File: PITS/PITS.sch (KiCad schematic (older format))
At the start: 47 parts, among them P1 CONN_02X20, P10 I2C, P11 I2C, P12 I2C, P13 I2C, P14 BATT, P2 BNC, P3 BNC, P4 BNC, P5 BNC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

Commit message: layout - work in progress - backup GPS antenne change
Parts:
- P2: footprint Connectors:SMA_Edge_small -> RF_Modules:MWSL1252
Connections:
- net GPIO22: now also D1.2 (A); no longer U4.14 (DIO0)
- net GPIO23: now also U4.14 (DIO0)
- net GPIO24: now also D2.2 (A)
- net GPIO25: now also U4.7 (DIO5)
- net GPIO27: no longer U4.7 (DIO5)
- net GPIO7(CE1): no longer U4.5 (nSS)
- net GPIO8(CE0): now also U4.5 (nSS)
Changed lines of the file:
@@
 Text Label 7100 1100 2    60   ~ 0
 GPIO10(MOSI0)
-Text Label 7000 1300 2    60   ~ 0
-GPIO7(CE1)
 Text Notes 9650 2550 2    100  ~ 20
 LORA/RFM9*
@@
 F 0 "P2" H 810 1120 50  0000 C CNN
 F 1 "BNC" V 910 940 50  0000 C CNN
-F 2 "Connectors:SMA_Edge_small" H 800 1000 50  0001 C CNN
+F 2 "RF_Modules:MWSL1252" H 800 1000 50  0001 C CNN
 F 3 "" H 800 1000 50  0000 C CNN
 	1    800  1000
@@
 Wire Wire Line
 	3500 1600 4100 1600
-Text Label 6900 2000 2    60   ~ 0
-GPIO27
-Text Label 6900 1500 2    60   ~ 0
+Text Label 2800 2900 2    60   ~ 0
 GPIO22
 $Comp
@@
 Text Label 2800 4100 2    60   ~ 0
 GPIO7(CE1)
+Text Label 7000 1300 2    60   ~ 0
+GPIO8(CE0)
+Text Label 2800 3300 2    60   ~ 0
+GPIO24
+Text Label 6900 2000 2    60   ~ 0
+GPIO25
+Text Label 6900 1500 2    60   ~ 0
+GPIO23
 $EndSCHEMATC

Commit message: layout - work in progress - RFM, LEDs, UBLOX
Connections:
- net D1: now also D1.2 (A), R14.2; no longer D1.1 (K), R14.1
- net D2: now also D2.2 (A), R15.2; no longer D2.1 (K), R15.1
- net D3: now also D3.2 (A), R20.2; no longer D3.1 (K), R20.1
- net D4: now also D4.2 (A), R21.2; no longer D4.1 (K), R21.1
- net D5: now also D5.2 (A), R22.2; no longer D5.1 (K), R22.1
- net D6: now also D6.2 (A), R23.2; no longer D6.1 (K), R23.1
- net GND: now also D1.1 (K), D2.1 (K), D3.1 (K), D4.1 (K), D5.1 (K), D6.1 (K); no longer R14.2, R15.2, R20.2, R21.2, R22.2, R23.2
- net GPIO12: no longer D3.2 (A)
- net GPIO13: now also R26.1
- net GPIO17: now also U4.14 (DIO0); no longer U3.4 (EN/PGM)
- net GPIO18: now also R14.1; no longer R26.1
- net GPIO22: now also R21.1; no longer D1.2 (A)
- net GPIO23: now also R20.1; no longer U4.14 (DIO0)
- net GPIO24: now also R22.1; no longer D2.2 (A)
- net GPIO25: now also R23.1; no longer U4.7 (DIO5)
- net GPIO27: now also R15.1
- net GPIO5: no longer D5.2 (A)
- net GPIO6: no longer D6.2 (A)
- net GPIO7(CE1): now also U4.5 (nSS); no longer D4.2 (A)
- net GPIO8(CE0): now also U4.7 (DIO5); no longer U4.5 (nSS)
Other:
- moved on the sheet: D1, D2, D3, D4, D5, D6, R14, R15, R20, R21, R22, R23
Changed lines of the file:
@@
 L LED D1
 U 1 1 58198207
-P 1700 2900
-F 0 "D1" H 1700 3000 50  0000 C CNN
-F 1 "OK_Green" H 1700 2800 50  0000 C CNN
-F 2 "LEDs:LED_0603" H 1700 2900 50  0001 C CNN
-F 3 "" H 1700 2900 50  0000 C CNN
-	1    1700 2900
+P 1200 2900
+F 0 "D1" H 1200 3000 50  0000 C CNN
+F 1 "OK_Green" H 1200 2800 50  0000 C CNN
+F 2 "LEDs:LED_0603" H 1200 2900 50  0001 C CNN
+F 3 "" H 1200 2900 50  0000 C CNN
+	1    1200 2900
 	1    0    0    -1
 $EndComp
@@
 L LED D2
 U 1 1 5819820E
-P 1700 3300
-F 0 "D2" H 1700 3400 50  0000 C CNN
-F 1 "WARN_Red" H 1700 3200 50  0000 C CNN
-F 2 "LEDs:LED_0603" H 1700 3300 50  0001 C CNN
-F 3 "" H 1700 3300 50  0000 C CNN
-	1    1700 3300
+P 1200 3300
+F 0 "D2" H 1200 3400 50  0000 C CNN
+F 1 "WARN_Red" H 1200 3200 50  0000 C CNN
+F 2 "LEDs:LED_0603" H 1200 3300 50  0001 C CNN
+F 3 "" H 1200 3300 50  0000 C CNN
+	1    1200 3300
 	1    0    0    -1
 $EndComp
@@
 L LED D3
 U 1 1 58198215
-P 1700 3700
-F 0 "D3" H 1700 3800 50  0000 C CNN
-F 1 "Inet_Green" H 1700 3600 50  0000 C CNN
-F 2 "LEDs:LED_0603" H 1700 3700 50  0001 C CNN
-F 3 "" H 1700 3700 50  0000 C CNN
-	1    1700 3700
+P 1200 3700
+F 0 "D3" H 1200 3800 50  0000 C CNN
+F 1 "Inet_Green" H 1200 3600 50  0000 C CNN
+F 2 "LEDs:LED_0603" H 1200 3700 50  0001 C CNN
+F 3 "" H 1200 3700 50  0000 C CNN
+	1    1200 3700
 	1    0    0    -1
 $EndComp
@@
 L R R14
 U 1 1 581983DD
-P 1150 2900
-F 0 "R14" V 1230 2900 50  0000 C CNN
-F 1 "330" V 1150 2900 50  0000 C CNN
-F 2 "Resistors_SMD:R_0603_HandSoldering" V 1080 2900 50  0001 C CNN
-F 3 "" H 1150 2900 50  0000 C CNN
-	1    1150 2900
+P 1750 2900
+F 0 "R14" V 1830 2900 50  0000 C CNN
+F 1 "330" V 1750 2900 50  0000 C CNN
+F 2 "Resistors_SMD:R_0603_HandSoldering" V 1680 2900 50  0001 C CNN
+F 3 "" H 1750 2900 50  0000 C CNN
+	1    1750 2900
 	0    1    1    0
 $EndComp
@@
 L R R15
 U 1 1 58198843
-P 1150 3300
-F 0 "R15" V 1230 3300 50  0000 C CNN
-F 1 "330" V 1150 3300 50  0000 C CNN
-F 2 "Resistors_SMD:R_0603_HandSoldering" V 1080 3300 50  0001 C CNN
-F 3 "" H 1150 3300 50  0000 C CNN
-	1    1150 3300
+P 1750 3300
+F 0 "R15" V 1830 3300 50  0000 C CNN
+F 1 "330" V 1750 3300 50  0000 C CNN
+F 2 "Resistors_SMD:R_0603_HandSoldering" V 1680 3300 50  0001 C CNN
+F 3 "" H 1750 3300 50  0000 C CNN
+	1    1750 3300
 	0    1    1    0
 $EndComp
@@
 L R R20
 U 1 1 581988DE
-P 1150 3700
-F 0 "R20" V 1230 3700 50  0000 C CNN
-F 1 "330" V 1150 3700 50  0000 C CNN
-F 2 "Resistors_SMD:R_0603_HandSoldering" V 1080 3700 50  0001 C CNN
-F 3 "" H 1150 3700 50  0000 C CNN
-	1    1150 3700
+P 1750 3700
+F 0 "R20" V 1830 3700 50  0000 C CNN
+F 1 "330" V 1750 3700 50  0000 C CNN
+F 2 "Resistors_SMD:R_0603_HandSoldering" V 1680 3700 50  0001 C CNN
+F 3 "" H 1750 3700 50  0000 C CNN
+	1    1750 3700
 	0    1    1    0
 $EndComp
@@
 L LED D4
 U 1 1 5819A39B
-P 1700 4100
-F 0 "D4" H 1700 4200 50  0000 C CNN
-F 1 "LAN_Yellow" H 1700 4000 50  0000 C CNN
-F 2 "LEDs:LED_0603" H 1700 4100 50  0001 C CNN
-F 3 "" H 1700 4100 50  0000 C CNN
-	1    1700 4100
+P 1200 4100
+F 0 "D4" H 1200 4200 50  0000 C CNN
+F 1 "LAN_Yellow" H 1200 4000 50  0000 C CNN
+F 2 "LEDs:LED_0603" H 1200 4100 50  0001 C CNN
+F 3 "" H 1200 4100 50  0000 C CNN
+	1    1200 4100
 	1    0    0    -1
 $EndComp
@@
 L LED D5
 U 1 1 5819A3A2
-P 1700 4500
-F 0 "D5" H 1700 4600 50  0000 C CNN
-F 1 "DATA0_Red" H 1700 4400 50  0000 C CNN
-F 2 "LEDs:LED_0603" H 1700 4500 50  0001 C CNN
-F 3 "" H 1700 4500 50  0000 C CNN
-	1    1700 4500
+P 1200 4500
+F 0 "D5" H 1200 4600 50  0000 C CNN
+F 1 "DATA0_Red" H 1200 4400 50  0000 C CNN
+F 2 "LEDs:LED_0603" H 1200 4500 50  0001 C CNN
+F 3 "" H 1200 4500 50  0000 C CNN
+	1    1200 4500
 	1    0    0    -1
 $EndComp
@@
 L LED D6
 U 1 1 5819A3A9
-P 1700 4900
-F 0 "D6" H 1700 5000 50  0000 C CNN
-F 1 "DATA1_Red" H 1700 4800 50  0000 C CNN
-F 2 "LEDs:LED_0603" H 1700 4900 50  0001 C CNN
-F 3 "" H 1700 4900 50  0000 C CNN
-	1    1700 4900
+P 1200 4900
+F 0 "D6" H 1200 5000 50  0000 C CNN
+F 1 "DATA1_Red" H 1200 4800 50  0000 C CNN
+F 2 "LEDs:LED_0603" H 1200 4900 50  0001 C CNN
+F 3 "" H 1200 4900 50  0000 C CNN
+	1    1200 4900
 	1    0    0    -1
 $EndComp
@@
 L R R21
 U 1 1 5819A3B0
-P 1150 4100
-F 0 "R21" V 1230 4100 50  0000 C CNN
-F 1 "330" V 1150 4100 50  0000 C CNN
-F 2 "Resistors_SMD:R_0603_HandSoldering" V 1080 4100 50  0001 C CNN
-F 3 "" H 1150 4100 50  0000 C CNN
-	1    1150 4100
+P 1750 4100
+F 0 "R21" V 1830 4100 50  0000 C CNN
+F 1 "330" V 1750 4100 50  0000 C CNN
+F 2 "Resistors_SMD:R_0603_HandSoldering" V 1680 4100 50  0001 C CNN
+F 3 "" H 1750 4100 50  0000 C CNN
+	1    1750 4100
 	0    1    1    0
 $EndComp
@@
 L R R22
 U 1 1 5819A3B7
-P 1150 4500
-F 0 "R22" V 1230 4500 50  0000 C CNN
-F 1 "330" V 1150 4500 50  0000 C CNN
-F 2 "Resistors_SMD:R_0603_HandSoldering" V 1080 4500 50  0001 C CNN
-F 3 "" H 1150 4500 50  0000 C CNN
-	1    1150 4500
+P 1750 4500
+F 0 "R22" V 1830 4500 50  0000 C CNN
+F 1 "330" V 1750 4500 50  0000 C CNN
+F 2 "Resistors_SMD:R_0603_HandSoldering" V 1680 4500 50  0001 C CNN
+F 3 "" H 1750 4500 50  0000 C CNN
+	1    1750 4500
 	0    1    1    0
 $EndComp
@@
 L R R23
 U 1 1 5819A3BE
-P 1150 4900
-F 0 "R23" V 1230 4900 50  0000 C CNN
-F 1 "330" V 1150 4900 50  0000 C CNN
-F 2 "Resistors_SMD:R_0603_HandSoldering" V 1080 4900 50  0001 C CNN
-F 3 "" H 1150 4900 50  0000 C CNN
-	1    1150 4900
+P 1750 4900
+F 0 "R23" V 1830 4900 50  0000 C CNN
+F 1 "330" V 1750 4900 50  0000 C CNN
+F 2 "Resistors_SMD:R_0603_HandSoldering" V 1680 4900 50  0001 C CNN
+F 3 "" H 1750 4900 50  0000 C CNN
+	1    1750 4900
 	0    1    1    0
 $EndComp
@@
 Text Label 4300 1300 2    60   ~ 0
 GPIO19(MISO1)
-Text Label 2800 4900 2    60   ~ 0
-GPIO6
-Text Label 2800 4500 2    60   ~ 0
-GPIO5
 Text Label 9800 4100 2    60   ~ 0
 GPIO2(SDA1)
@@
 	0    1    1    0
 $EndComp
-Text Label 6800 6100 2    60   ~ 0
-GPIO17
 Text Label 6800 6000 2    60   ~ 0
 GPIO14(TXD0)
-Text Label 3300 6100 2    60   ~ 0
-GPIO18
 Text Notes 6850 7050 2    100  ~ 20
 UKHAS
@@
 Connection ~ 4000 4200
 Wire Wire Line
-	1300 2900 1500 2900
-Wire Wire Line
-	1500 3300 1300 3300
-Wire Wire Line
-	1300 3700 1500 3700
+	1400 2900 1600 2900
+Wire Wire Line
+	1600 3300 1400 3300
+Wire Wire Line
+	1400 3700 1600 3700
 Wire Wire Line
 	900  2900 1000 2900
@@
 	900  3700 1000 3700
 Wire Wire Line
-	1300 4100 1500 4100
-Wire Wire Line
-	1500 4500 1300 4500
-Wire Wire Line
-	1300 4900 1500 4900
+	1400 4100 1600 4100
+Wire Wire Line
+	1600 4500 1400 4500
+Wire Wire Line
+	1400 4900 1600 4900
 Wire Wire Line
 	900  4100 1000 4100
@@
 Wire Wire Line
 	3500 1600 4100 1600
-Text Label 2800 2900 2    60   ~ 0
+Text Label 2800 4100 2    60   ~ 0
 GPIO22
 $Comp
@@
 Text Label 2500 6100 0    30   ~ 0
 HX1-TXD
-Text Label 1400 2900 0    30   ~ 0
+Text Label 1500 2900 0    30   ~ 0
 D1
-Text Label 1400 3300 0    30   ~ 0
+Text Label 1500 3300 0    30   ~ 0
 D2
-Text Label 1400 3700 0    30   ~ 0
+Text Label 1500 3700 0    30   ~ 0
 D3
-Text Label 1400 4100 0    30   ~ 0
+Text Label 1500 4100 0    30   ~ 0
 D4
-Text Label 1400 4500 0    30   ~ 0
+Text Label 1500 4500 0    30   ~ 0
 D5
-Text Label 1400 4900 0    30   ~ 0
+Text Label 1500 4900 0    30   ~ 0
 D6
 $Comp
@@
 	1    0    0    -1
 $EndComp
+Text Label 6900 2000 2    60   ~ 0
+GPIO8(CE0)
+Text Label 2800 4500 2    60   ~ 0
+GPIO24
+Text Label 7000 1300 2    60   ~ 0
+GPIO7(CE1)
+Text Label 3300 6100 2    60   ~ 0
+GPIO13
+Text Label 6900 1500 2    60   ~ 0
+GPIO17
+Text Label 2800 4900 2    60   ~ 0
+GPIO25
 Text Label 2800 3700 2    60   ~ 0
-GPIO12
-Text Label 2800 4100 2    60   ~ 0
-GPIO7(CE1)
-Text Label 7000 1300 2    60   ~ 0
-GPIO8(CE0)
+GPIO23
 Text Label 2800 3300 2    60   ~ 0
-GPIO24
-Text Label 6900 2000 2    60   ~ 0
-GPIO25
-Text Label 6900 1500 2    60   ~ 0
-GPIO23
+GPIO27
+Text Label 2800 2900 2    60   ~ 0
+GPIO18
 $EndSCHEMATC

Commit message: neue Pinbelegung
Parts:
- removed R5: 10k, Resistors_SMD:R_0603_HandSoldering, symbol R
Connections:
- net GPIO12: no longer U2.4 (TimePulse)
- net GPIO14(TXD0): no longer U2.3 (RXD)
- net GPIO15(RXD0): no longer U2.2 (TXD)
- net GPIO16(CE2): no longer U2.17 (SCL)
- net GPIO17: now also U2.4 (TimePulse); no longer U4.14 (DIO0)
- net GPIO18: now also U2.16 (SDA); no longer R14.1
- net GPIO19(MISO1): no longer U2.16 (SDA)
- net GPIO22: now also U1.4 (EN); no longer R21.1
- net GPIO23: now also R14.1; no longer R20.1
- net GPIO24: now also R15.1; no longer R22.1
- net GPIO25: now also R20.1; no longer R23.1, U1.4 (EN)
- net GPIO27: now also U4.14 (DIO0); no longer R15.1
- net GPIO4: now also U2.17 (SCL)
- no-connect marks 10 -> 12
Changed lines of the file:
@@
 	0    1    1    0
 $EndComp
-Text Label 4300 1300 2    60   ~ 0
-GPIO19(MISO1)
 Text Label 9800 4100 2    60   ~ 0
 GPIO2(SDA1)
@@
 	0    1    1    0
 $EndComp
-Text Label 6800 6000 2    60   ~ 0
-GPIO14(TXD0)
 Text Notes 6850 7050 2    100  ~ 20
 UKHAS
@@
 	1    0    0    -1
 $EndComp
-Text Label 4500 1100 2    60   ~ 0
-GPIO14(TXD0)
-Text Label 4500 1000 2    60   ~ 0
-GPIO15(RXD0)
-$Comp
-L R R5
-U 1 1 581C7F21
-P 3950 800
-F 0 "R5" V 4030 800 50  0000 C CNN
-F 1 "10k" V 3950 800 50  0000 C CNN
-F 2 "Resistors_SMD:R_0603_HandSoldering" V 3880 800 50  0001 C CNN
-F 3 "" H 3950 800 50  0000 C CNN
-	1    3950 800
-	0    1    1    0
-$EndComp
-Text Label 4500 800  2    60   ~ 0
-GPIO17
 Text Notes 4550 2550 2    100  ~ 20
 GPS
@@
 	2500 6100 2600 6100
 Wire Wire Line
-	6100 6000 6800 6000
-Wire Wire Line
 	2900 6100 3300 6100
 Wire Wire Line
@@
 Wire Wire Line
 	800  1200 800  2200
-Wire Wire Line
-	3500 1100 4500 1100
-Wire Wire Line
-	3500 1300 4300 1300
-Wire Wire Line
-	3500 1400 4300 1400
-Wire Wire Line
-	4500 1000 3500 1000
-Wire Wire Line
-	4500 800  4100 800
-Wire Wire Line
-	3600 1000 3600 800
-Wire Wire Line
-	3600 800  3800 800
-Connection ~ 3600 1000
 Wire Notes Line
 	4700 600  9700 600
@@
 Wire Wire Line
 	8100 5800 8300 5800
-Text Label 3300 6200 2    60   ~ 0
-GPIO25
-Text Label 4300 1400 2    60   ~ 0
-GPIO16(CE2)
-Text Label 4100 1600 2    60   ~ 0
-GPIO12
 Wire Wire Line
 	3500 1600 4100 1600
-Text Label 2800 4100 2    60   ~ 0
-GPIO22
 $Comp
 L BME280 U8
@@
 	1    0    0    -1
 $EndComp
+Wire Wire Line
+	3500 1400 4300 1400
+Wire Wire Line
+	3500 1300 4300 1300
+NoConn ~ 3500 1000
+NoConn ~ 3500 1100
+Wire Wire Line
+	6100 6000 6800 6000
+Text Label 4100 1600 2    60   ~ 0
+GPIO17
+Text Label 4300 1400 2    60   ~ 0
+GPIO4
+Text Label 4300 1300 2    60   ~ 0
+GPIO18
+Text Label 6900 1500 2    60   ~ 0
+GPIO27
 Text Label 6900 2000 2    60   ~ 0
 GPIO8(CE0)
-Text Label 2800 4500 2    60   ~ 0
-GPIO24
 Text Label 7000 1300 2    60   ~ 0
 GPIO7(CE1)
+Text Label 2800 2900 2    60   ~ 0
+GPIO23
+Text Label 2800 3300 2    60   ~ 0
+GPIO24
+Text Label 2800 3700 2    60   ~ 0
+GPIO25
+Text Label 3300 6200 2    60   ~ 0
+GPIO22
 Text Label 3300 6100 2    60   ~ 0
 GPIO13
-Text Label 6900 1500 2    60   ~ 0
-GPIO17
-Text Label 2800 4900 2    60   ~ 0
-GPIO25
-Text Label 2800 3700 2    60   ~ 0
-GPIO23
-Text Label 2800 3300 2    60   ~ 0
-GPIO27
-Text Label 2800 2900 2    60   ~ 0
-GPIO18
+Text Label 6800 6000 2    60   ~ 0
+GPIO14(TXD0)
 $EndSCHEMATC

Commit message: Layout - MTX2, HX1 and LEDs
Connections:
- net GPIO12: now also R21.1
- net GPIO5: now also R22.1
- net GPIO6: now also R23.1
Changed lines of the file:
@@
 Text Label 6800 6000 2    60   ~ 0
 GPIO14(TXD0)
+Text Label 2800 4500 2    60   ~ 0
+GPIO5
+Text Label 2800 4900 2    60   ~ 0
+GPIO6
+Text Label 2800 4100 2    60   ~ 0
+GPIO12
 $EndSCHEMATC

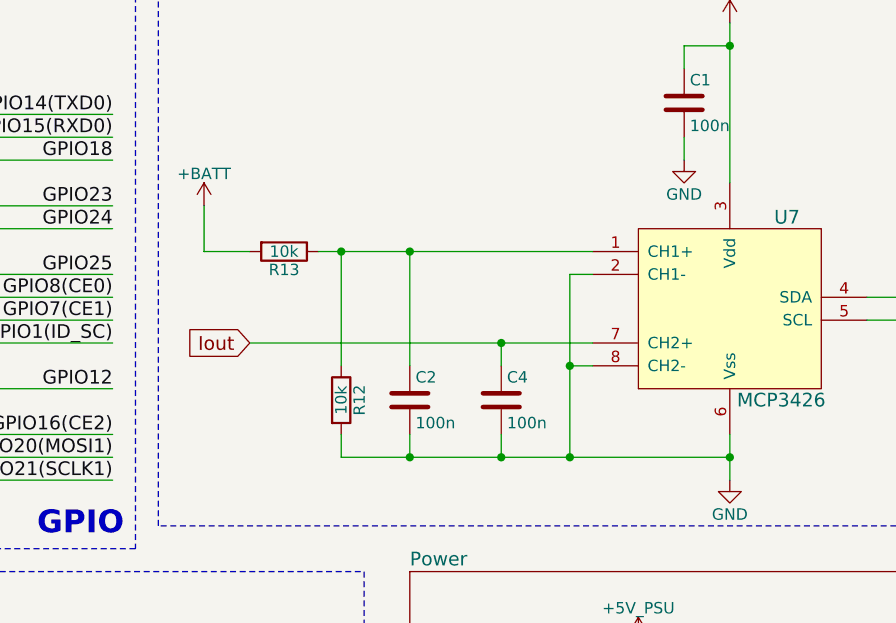
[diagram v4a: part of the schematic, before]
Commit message: ADC, BME280 and power switch
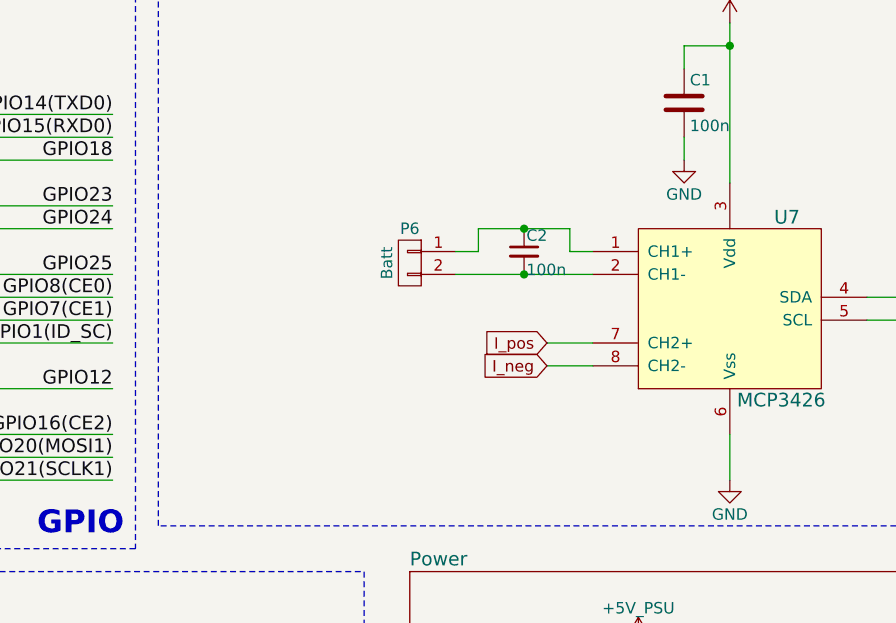
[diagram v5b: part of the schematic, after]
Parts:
- removed C2, C4: 100n, Capacitors_SMD:C_0603_HandSoldering, symbol C
- removed R12, R13: 10k, Resistors_SMD:R_0603_HandSoldering, symbol R
- added C2: 100n, Capacitors_SMD:C_0603_HandSoldering, symbol C_Small
- added P6: Batt, Connectors:SMD_2_xsmall, symbol CONN_01X02
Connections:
- net GND: no longer U7.2 (CH1-), U7.8 (CH2-)
- net at U7.1 (CH1+): now also C2.1, P6.1 (P1)
- net Iout renamed I_pos
- new net: C2.2, P6.2 (P2), U7.2 (CH1-)
- new net I_neg: U7.8 (CH2-)

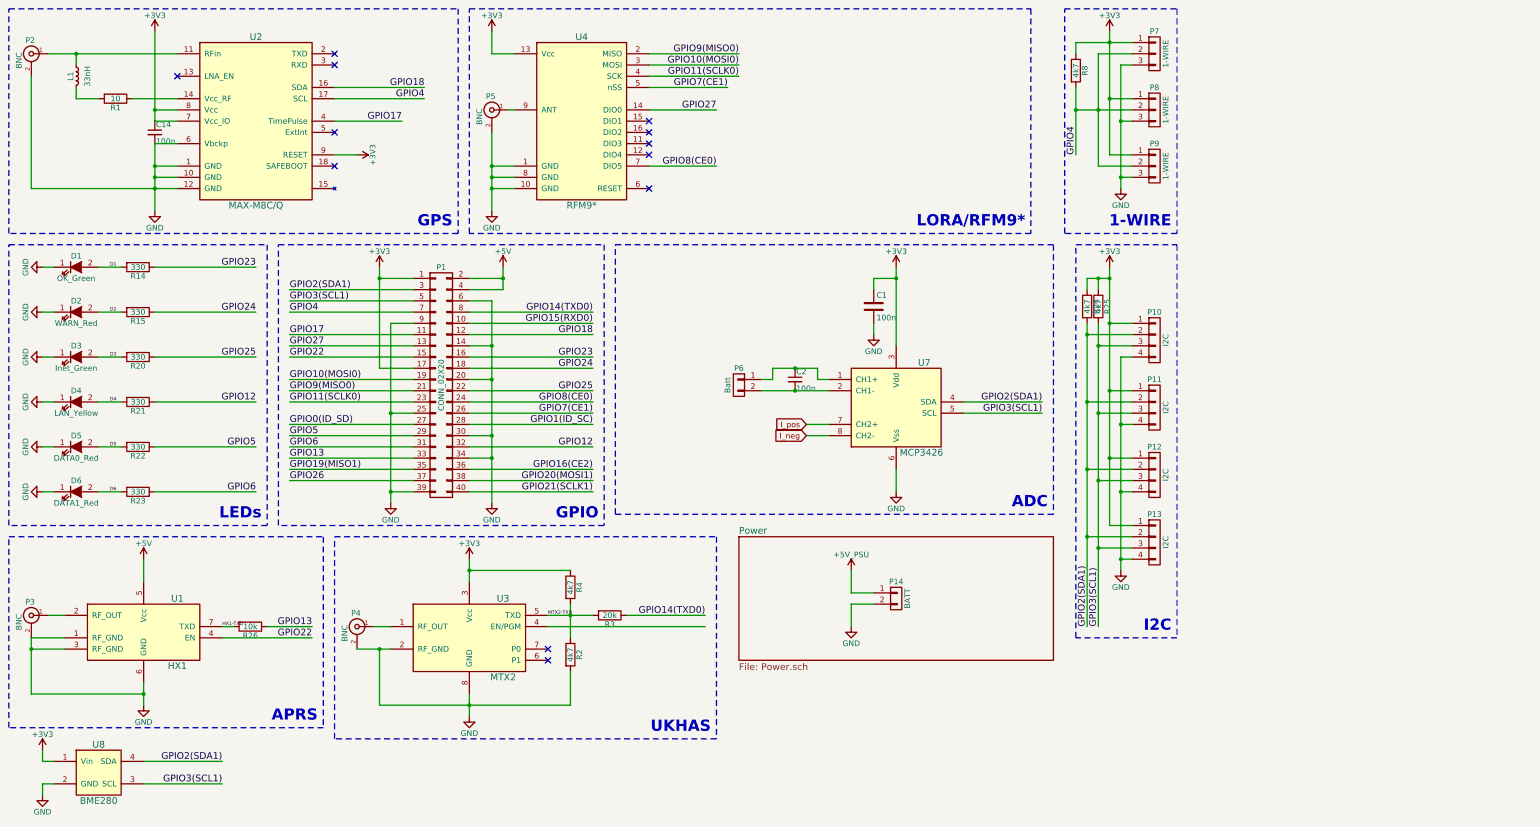
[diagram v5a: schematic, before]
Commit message: Layout almost finished
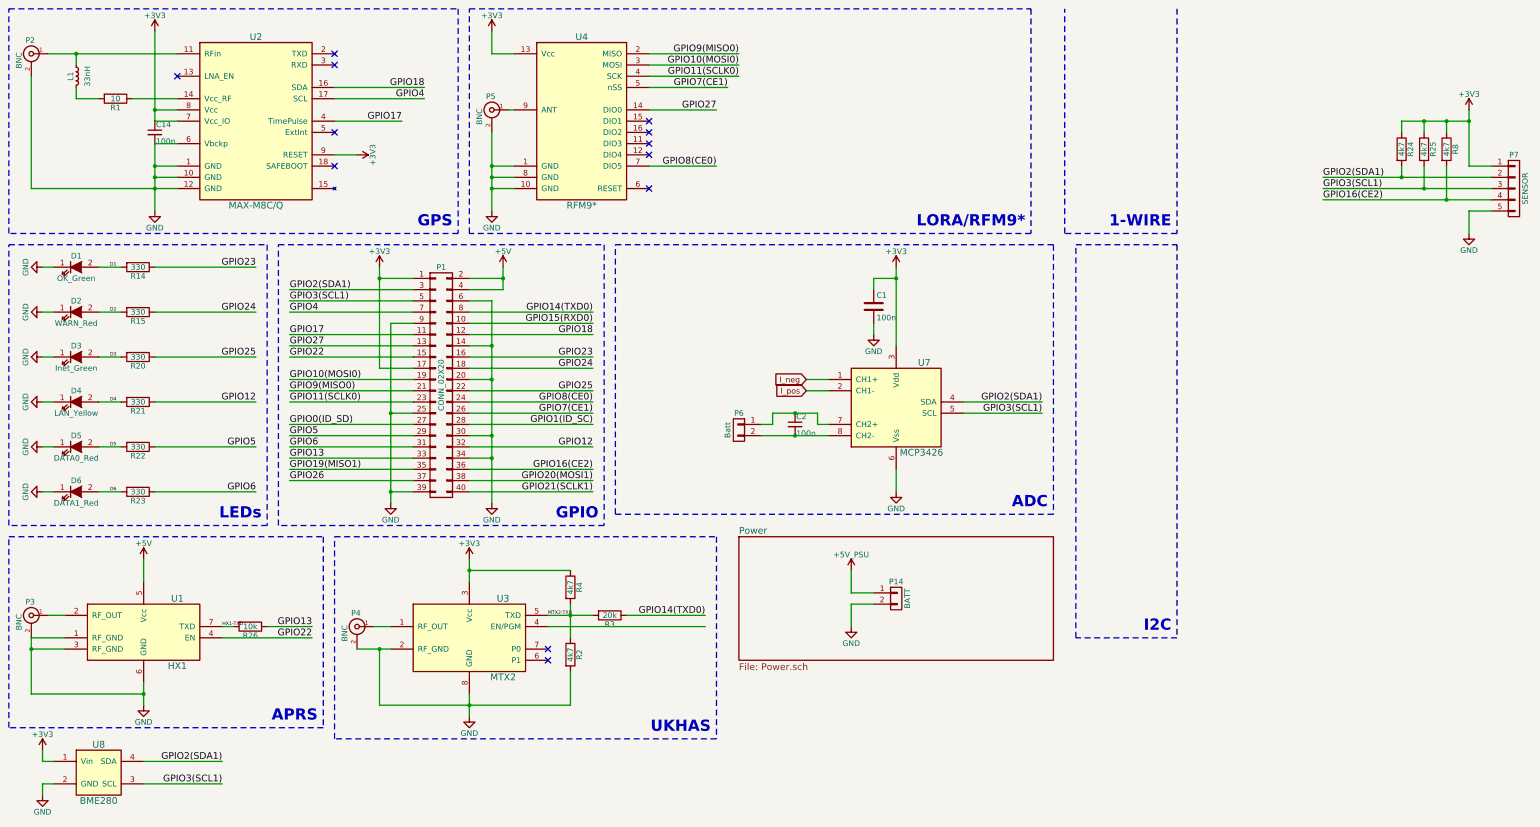
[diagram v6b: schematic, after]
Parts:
- removed P10, P11, P12, P13: I2C, Socket_Strips:Socket_Strip_Straight_1x04, symbol CONN_01X04
- removed P7, P8, P9: 1-WIRE, Socket_Strips:Socket_Strip_Straight_1x03, symbol CONN_01X03
- added P7: SENSOR, Connectors:SMD_5_xsmall, symbol CONN_01X05
- P14: footprint Connectors:SMD_2_small -> Pin_Headers:Pin_Header_Straight_1x02_Pitch2.00mm
- P6: footprint Connectors:SMD_2_xsmall -> Pin_Headers:Pin_Header_Straight_1x02_Pitch2.00mm
- U8: footprint RF_Modules:BME280 -> RF_Modules:BME280_edit
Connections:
- net +3V3: now also P7.1 (P1)
- net GND: now also P7.5 (P5)
- net GPIO16(CE2): now also R8.2, P7.4 (P4)
- net GPIO2(SDA1): now also P7.2 (P2)
- net GPIO3(SCL1): now also P7.3 (P3)
- net GPIO4: no longer R8.2
- net I_neg: now also U7.1 (CH1+); no longer U7.8 (CH2-)
- net I_pos: now also U7.2 (CH1-); no longer U7.7 (CH2+)
- net at C2.1, P6.1 (P1): now also U7.7 (CH2+); no longer U7.1 (CH1+)
- net at C2.2, P6.2 (P2): now also U7.8 (CH2-); no longer U7.2 (CH1-)
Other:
- moved on the sheet: C2, P6, R24, R25, R8
